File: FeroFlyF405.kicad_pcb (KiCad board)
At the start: 4 copper layers, 50 x 65 mm, 154 parts, among them J302 SM04B-GHS-TB(LF)(SN), J601 SM04B-GHS-TB(LF)(SN), J801 SM04B-GHS-TB(LF)(SN), J802 SM06B-GHS-TB(LF)(SN), J803 SM04B-GHS-TB(LF)(SN), J804 SM04B-GHS-TB(LF)(SN), J805 SM06B-GHS-TB(LF)(SN), J901 Conn_01x03_Pin, J902 Conn_01x03_Pin, J903 Conn_01x03_Pin, J904 Conn_01x03_Pin, J905 Conn_01x03_Pin, J906 Conn_01x03_Pin, J907 Conn_01x03_Pin, J908 Conn_01x03_Pin, J909 Conn_01x03_Pin, J910 Conn_01x03_Pin, J911 Conn_01x03_Pin, J912 Conn_01x03_Pin, J913 12402012E212A, J914 SM04B-GHS-TB(LF)(SN), SW301 SW_Push, SW302 SW_Push, U201 AP62200WU-7, U202 TLV75733PDRV, U301 STM32F405RGTx, U501 LSM6DSL, U502 DPS368, U601 SN65HVD230DR, U901 USBLC6-2P6, Y301 24MHz

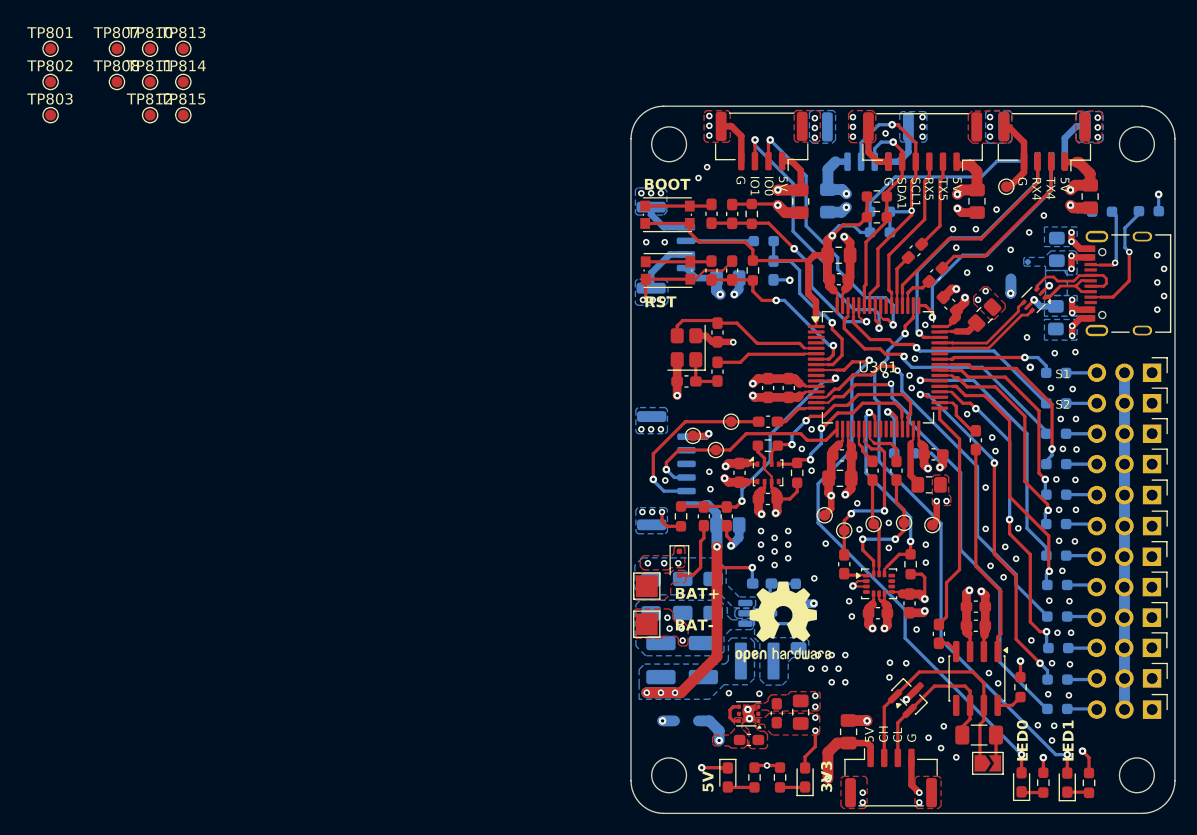
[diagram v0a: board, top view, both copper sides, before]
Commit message: feat: add remaing silkscreen & Logos
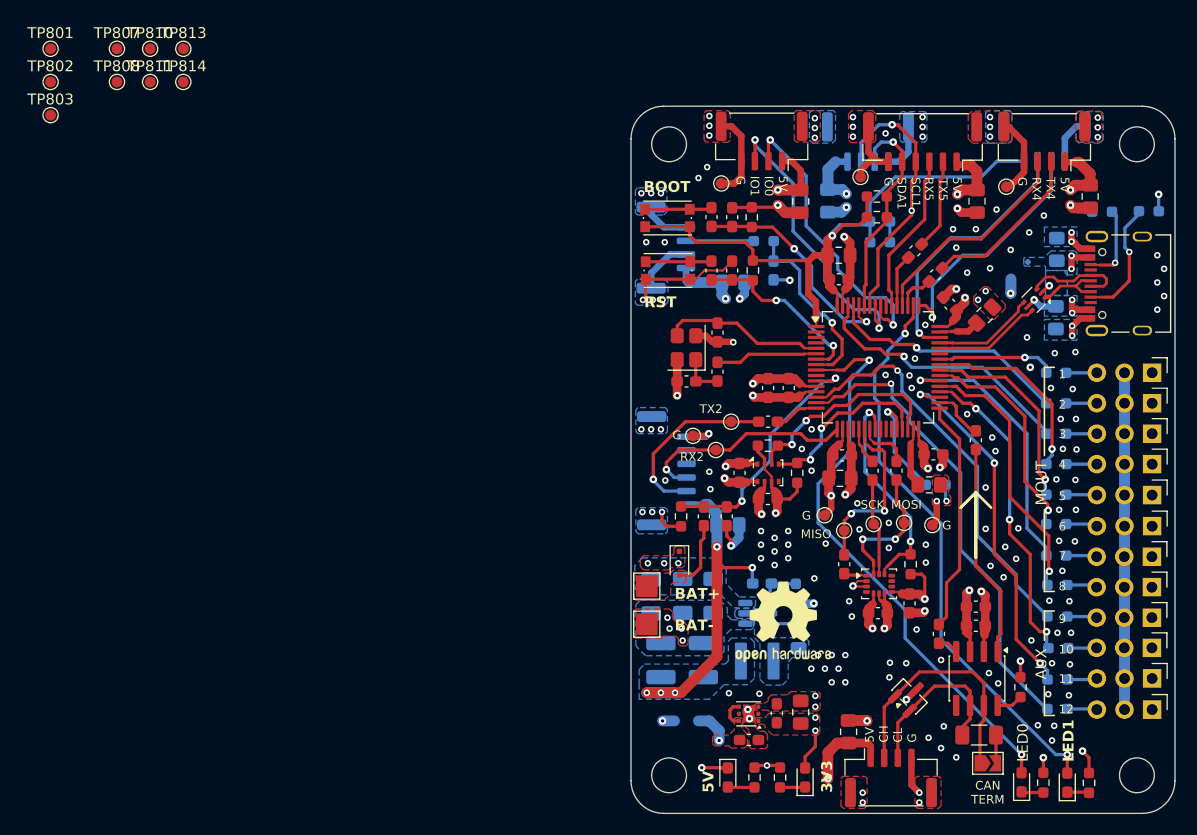
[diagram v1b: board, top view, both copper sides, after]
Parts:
- added G***: LOGO, NextPCB-Logo:NextPCB-Logo, B.Cu at (151.2, 114.2)
- moved TP815 62.5 mm to (149.1, 60.5)
- moved TP812 52.9 mm to (136.3, 61.1)
- moved R316 4.09 mm to (156.0, 88.8)
- moved R314 0.90 mm to (150.9, 66.5)
- moved R312 0.90 mm to (150.9, 64.6)
- moved C903 0.64 mm to (137.4, 70.2)
- moved C302 0.30 mm to (137.3, 64.2)
- moved R304 0.30 mm to (139.1, 64.2)
- moved SW302 0.30 mm to (131.3, 64.3)
- moved R302 0.30 mm to (135.4, 64.2)
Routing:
- net GND: track 155.0 -> 159.5 mm
- net /MCU/D_BOOT1: track 6.16 -> 10.2 mm
- net /IO/D_I2C1_SCL: track 28.8 -> 26.9 mm
- net +5V: track 102.6 -> 104.1 mm
- net +3V3: track 229.9 -> 230.6 mm
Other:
- board text added: "1"
- board text added: "10"
- board text added: "11"
- board text added: "12"
- board text added: "2"
- board text added: "3"
- board text added: "4"
- board text added: "5"
- board text added: "6"
- board text added: "7"
- board text added: "8"
- board text added: "9"
- board text added: "AUX"
- board text added: "CAN TERM"
- board text added: "CUR"
- board text added: "FeroFlyF405"
- board text added: "MISO"
- board text added: "MOSI"
- board text added: "MOUT"
- board text added: "REV:1"
- board text added: "SCK"
- board text removed: "S1"
- board text removed: "S2"

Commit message: refactor: add & tweak silkscreen
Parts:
- added REF**: OSHW-Symbol_8.9x8mm_SilkScreen, Symbol:OSHW-Symbol_8.9x8mm_SilkScreen, B.Cu at (150.9, 75.0)
- moved R604 1.61 mm to (156.7, 100.9)
- moved JP601 0.70 mm to (160.1, 114.4)
- moved C304 0.10 mm to (135.9, 74.9)
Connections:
- net /Peripherals/CAN & LEDs/D_CANTR renamed /Peripherals/CAN & LEDs/CAN+R
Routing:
- net GND: track 159.5 -> 194.8 mm, vias 189 -> 210
- net /MCU/D_CAN2RX: track 21.4 -> 19.6 mm
- net /IO/D_PINIO1: track 27.3 -> 26.2 mm
- net /Peripherals/CAN & LEDs/D_CANR: track 1.91 -> 2.82 mm

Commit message: feat: add last test point & perform final check
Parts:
- removed the TP801 at (74.7, 48.7)
- removed the TP802 at (74.7, 51.8)
- removed TP803, TP808, TP810, TP811, TP813, TP814: TestPoint, TestPoint:TestPoint_Pad_D1.0mm
- removed the TP807 at (80.8, 48.7)
- added G: TestPoint, TestPoint:TestPoint_Pad_D1.0mm, B.Cu at (153.9, 60.8)
- renumbered C802 to C801, C801 to C802, C805 to C804, C804 to C805, J802 to J801, J801 to J802, TP815 to TP801, TP809 to TP802, TP812 to TP804, TP804 to TP805, TP805 to TP806, TP806 to TP807
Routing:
- net /IO/D_I2C1_SCL: track 26.9 -> 29.5 mm
- net GND: track 194.8 -> 197.2 mm

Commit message: feat: add gerbers
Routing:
- net GND: vias 210 -> 213
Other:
- rule pad_to_mask_clearance: 0.06 -> 0
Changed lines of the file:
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@@
 			(dielectric_constraints no)
 		)
-		(pad_to_mask_clearance 0.06)
+		(pad_to_mask_clearance 0)
 		(allow_soldermask_bridges_in_footprints yes)
 		(tenting
@@
 			(plot_on_all_layers_selection 0x00000000_00000000_00000000_00000000)
 			(disableapertmacros no)
-			(usegerberextensions no)
+			(usegerberextensions yes)
 			(usegerberattributes yes)
 			(usegerberadvancedattributes yes)
@@
 			(outputformat 1)
 			(mirror no)
-			(drillshape 1)
+			(drillshape 0)
 			(scaleselection 1)
-			(outputdirectory "")
+			(outputdirectory "Gerbers")
 		)
 	)
@@
 	)
 	(via
+		(at 159.8 67)
+		(size 0.6)
+		(drill 0.3)
+		(layers "F.Cu" "B.Cu")
+		(free yes)
+		(net "GND")
+	)
+	(via
 		(at 149.7 110.5)
 		(size 0.7)
@@
 	)
 	(via
+		(at 152.75 63.5)
+		(size 0.6)
+		(drill 0.3)
+		(layers "F.Cu" "B.Cu")
+		(free yes)
+		(net "GND")
+	)
+	(via
 		(at 144.9 55.1)
 		(size 0.6)
@@
 	)
 	(via
+		(at 155.65 64.7)
+		(size 0.6)
+		(drill 0.3)
+		(layers "F.Cu" "B.Cu")
+		(free yes)
+		(net "GND")
+	)
+	(via
 		(at 154.8 55)
 		(size 0.6)
@@
 	)
 	(segment
-		(start 151.6 73.6)
-		(end 152.1 74.1)
-		(width 0.3)
-		(layer "F.Cu")
-		(net "/IO/D_PINIO0")
-	)
-	(segment
-		(start 150.95 72.325)
-		(end 150.95 73.35)
-		(width 0.2)
-		(layer "F.Cu")
-		(net "/IO/D_PINIO0")
-	)
-	(segment
-		(start 151.3 73.6)
-		(end 151.6 73.6)
-		(width 0.3)
-		(layer "F.Cu")
-		(net "/IO/D_PINIO0")
-	)
-	(segment
-		(start 140.6375 57.2625)
-		(end 140.6375 59.05)
-		(width 0.3)
-		(layer "F.Cu")
-		(net "/IO/D_PINIO0")
-	)
-	(segment
-		(start 150.95 73.35)
-		(end 151.2 73.6)
-		(width 0.2)
-		(layer "F.Cu")
-		(net "/IO/D_PINIO0")
-	)
-	(segment
-		(start 140.8 57.1)
-		(end 140.6375 57.2625)
-		(width 0.3)
-		(layer "F.Cu")
-		(net "/IO/D_PINIO0")
-	)
-	(segment
-		(start 151.2 73.6)
-		(end 151.3 73.6)
-		(width 0.2)
-		(layer "F.Cu")
-		(net "/IO/D_PINIO0")
-	)
-	(via
-		(at 152.1 74.1)
-		(size 0.7)
-		(drill 0.3)
-		(layers "F.Cu" "B.Cu")
-		(net "/IO/D_PINIO0")
-	)
-	(via
-		(at 140.8 57.1)
-		(size 0.7)
-		(drill 0.3)
-		(layers "F.Cu" "B.Cu")
-		(net "/IO/D_PINIO0")
-	)
-	(segment
-		(start 152.1 71.5)
-		(end 149 68.4)
-		(width 0.3)
-		(layer "B.Cu")
-		(net "/IO/D_PINIO0")
-	)
-	(segment
-		(start 149 68.4)
-		(end 147.5 68.4)
-		(width 0.3)
-		(layer "B.Cu")
-		(net "/IO/D_PINIO0")
-	)
-	(segment
-		(start 152.1 74.1)
-		(end 152.1 71.5)
-		(width 0.3)
-		(layer "B.Cu")
-		(net "/IO/D_PINIO0")
-	)
-	(segment
-		(start 147.5 68.4)
-		(end 144.1 65)
-		(width 0.3)
-		(layer "B.Cu")
-		(net "/IO/D_PINIO0")
-	)
-	(segment
-		(start 144.1 65)
-		(end 144.1 60.4)
-		(width 0.3)
-		(layer "B.Cu")
-		(net "/IO/D_PINIO0")
-	)
-	(segment
-		(start 144.1 60.4)
-		(end 140.8 57.1)
-		(width 0.3)
-		(layer "B.Cu")
-		(net "/IO/D_PINIO0")
-	)
-	(segment
 		(start 137.925 110.5)
 		(end 137.4 110.5)
@@
 	)
 	(segment
+		(start 151.6 73.6)
+		(end 152.1 74.1)
+		(width 0.3)
+		(layer "F.Cu")
+		(net "/IO/D_PINIO0")
+	)
+	(segment
+		(start 150.95 72.325)
+		(end 150.95 73.35)
+		(width 0.2)
+		(layer "F.Cu")
+		(net "/IO/D_PINIO0")
+	)
+	(segment
+		(start 151.3 73.6)
+		(end 151.6 73.6)
+		(width 0.3)
+		(layer "F.Cu")
+		(net "/IO/D_PINIO0")
+	)
+	(segment
+		(start 140.6375 57.2625)
+		(end 140.6375 59.05)
+		(width 0.3)
+		(layer "F.Cu")
+		(net "/IO/D_PINIO0")
+	)
+	(segment
+		(start 150.95 73.35)
+		(end 151.2 73.6)
+		(width 0.2)
+		(layer "F.Cu")
+		(net "/IO/D_PINIO0")
+	)
+	(segment
+		(start 140.8 57.1)
+		(end 140.6375 57.2625)
+		(width 0.3)
+		(layer "F.Cu")
+		(net "/IO/D_PINIO0")
+	)
+	(segment
+		(start 151.2 73.6)
+		(end 151.3 73.6)
+		(width 0.2)
+		(layer "F.Cu")
+		(net "/IO/D_PINIO0")
+	)
+	(via
+		(at 152.1 74.1)
+		(size 0.7)
+		(drill 0.3)
+		(layers "F.Cu" "B.Cu")
+		(net "/IO/D_PINIO0")
+	)
+	(via
+		(at 140.8 57.1)
+		(size 0.7)
+		(drill 0.3)
+		(layers "F.Cu" "B.Cu")
+		(net "/IO/D_PINIO0")
+	)
+	(segment
+		(start 152.1 71.5)
+		(end 149 68.4)
+		(width 0.3)
+		(layer "B.Cu")
+		(net "/IO/D_PINIO0")
+	)
+	(segment
+		(start 149 68.4)
+		(end 147.5 68.4)
+		(width 0.3)
+		(layer "B.Cu")
+		(net "/IO/D_PINIO0")
+	)
+	(segment
+		(start 152.1 74.1)
+		(end 152.1 71.5)
+		(width 0.3)
+		(layer "B.Cu")
+		(net "/IO/D_PINIO0")
+	)
+	(segment
+		(start 147.5 68.4)
+		(end 144.1 65)
+		(width 0.3)
+		(layer "B.Cu")
+		(net "/IO/D_PINIO0")
+	)
+	(segment
+		(start 144.1 65)
+		(end 144.1 60.4)
+		(width 0.3)
+		(layer "B.Cu")
+		(net "/IO/D_PINIO0")
+	)
+	(segment
+		(start 144.1 60.4)
+		(end 140.8 57.1)
+		(width 0.3)
+		(layer "B.Cu")
+		(net "/IO/D_PINIO0")
+	)
+	(segment
 		(start 150.45 73.65)
 		(end 150.5 73.7)
@@
 	)
 	(segment
-		(start 163.9 113.6)
-		(end 153.2 102.9)
+		(start 152.6 102.3)
+		(end 152.6 99.7)
 		(width 0.3)
 		(layer "B.Cu")
@@
 	)
 	(segment
-		(start 145.2 92.3)
-		(end 145.2 88.7)
+		(start 149.9 77.4)
+		(end 149.9 77.35)
 		(width 0.3)
 		(layer "B.Cu")
@@
 	)
 	(segment
-		(start 153.2 100.3)
-		(end 145.2 92.3)
+		(start 145.2 88.7)
+		(end 148.1 85.8)
 		(width 0.3)
 		(layer "B.Cu")
@@
 	)
 	(segment
-		(start 149.9 77.4)
-		(end 149.9 77.35)
+		(start 148.1 79.2)
+		(end 149.9 77.4)
 		(width 0.3)
 		(layer "B.Cu")
@@
 	)
 	(segment
-		(start 148.1 79.2)
-		(end 149.9 77.4)
+		(start 163.9 113.6)
+		(end 152.6 102.3)
 		(width 0.3)
 		(layer "B.Cu")
@@
 	)
 	(segment
-		(start 153.2 102.9)
-		(end 153.2 100.3)
+		(start 152.6 99.7)
+		(end 145.2 92.3)
 		(width 0.3)
 		(layer "B.Cu")
@@
 	)
 	(segment
-		(start 148.1 85.8)
-		(end 148.1 79.2)
+		(start 145.2 92.3)
+		(end 145.2 88.7)
 		(width 0.3)
 		(layer "B.Cu")
@@
 	)
 	(segment
-		(start 145.2 88.7)
-		(end 148.1 85.8)
+		(start 148.1 85.8)
+		(end 148.1 79.2)
 		(width 0.3)
 		(layer "B.Cu")
